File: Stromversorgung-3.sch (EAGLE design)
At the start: 28 parts, among them IC1 TI-INA226, U1 TSR2-2450, U2 TSR1-2433, U3 TSR1-2450, U4 TSR1-24120, X1 Ein/Aus, X2 MAC64L, X3 Eingang

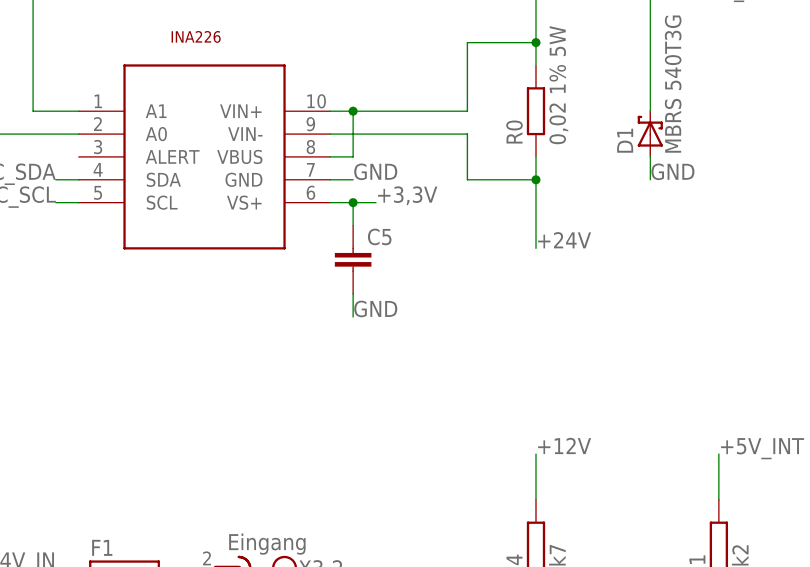
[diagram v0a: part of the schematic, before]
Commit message: Werte von Bauteilen angepasst
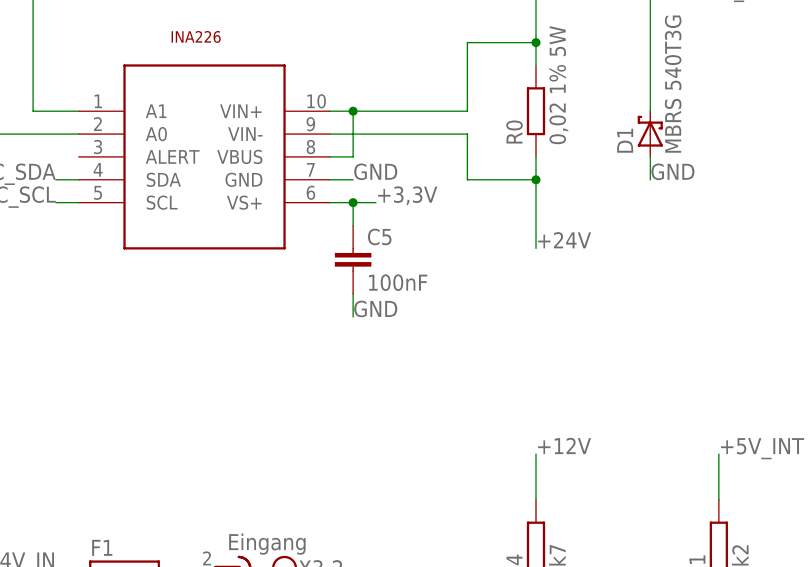
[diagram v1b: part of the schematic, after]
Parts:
- C5: value (none) -> 100nF
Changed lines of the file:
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@@
 <part name="IC1" library="FaBo-Sensor" deviceset="TI-INA226" device=""/>
 <part name="R0" library="rcl" deviceset="R-EU_" device="R2512" value="0,02 1% 5W"/>
-<part name="C5" library="rcl" deviceset="C-EU" device="C1206"/>
+<part name="C5" library="rcl" deviceset="C-EU" device="C1206" value="100nF"/>
 <part name="A1" library="SparkFun-Jumpers" deviceset="JUMPER-SMT_3_NO" device="_NO-SILK"/>
 <part name="A0" library="SparkFun-Jumpers" deviceset="JUMPER-SMT_3_NO" device="_NO-SILK"/>
